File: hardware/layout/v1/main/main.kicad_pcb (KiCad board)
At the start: 4 copper layers, 32 x 52 mm, 47 parts, among them J1 12-32V + RS485, J2 Crown board, J3 Probe board, J4 PMSA003I PM, J5 Power board, Q1 AO3400A, SW1 SERVICE, U2 LM66100, U3 XIAO ESP32C6, U4 ADS1115IDGSR, U5 LSM6DS3TR-C, U7 SP3485EN-L/TR

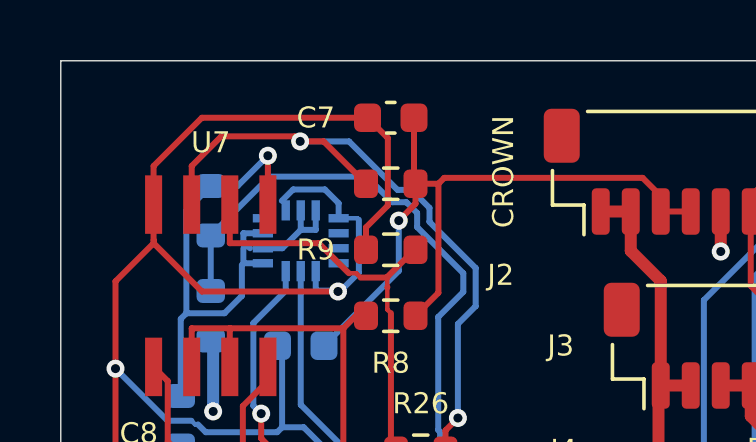
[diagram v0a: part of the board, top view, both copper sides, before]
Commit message: Update dome PCB to Genicom GUVB-C21SD/GUVA-C22SD photodiodes with TLV9062 transimpedance and ADS1115 ADC, increase diameter to Ø 15.6 mm
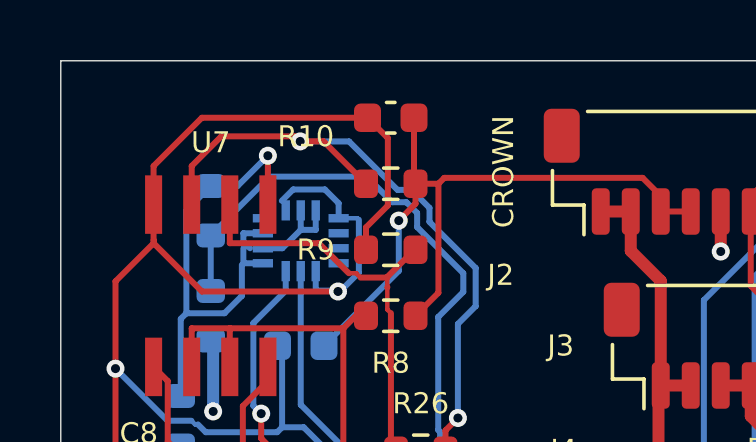
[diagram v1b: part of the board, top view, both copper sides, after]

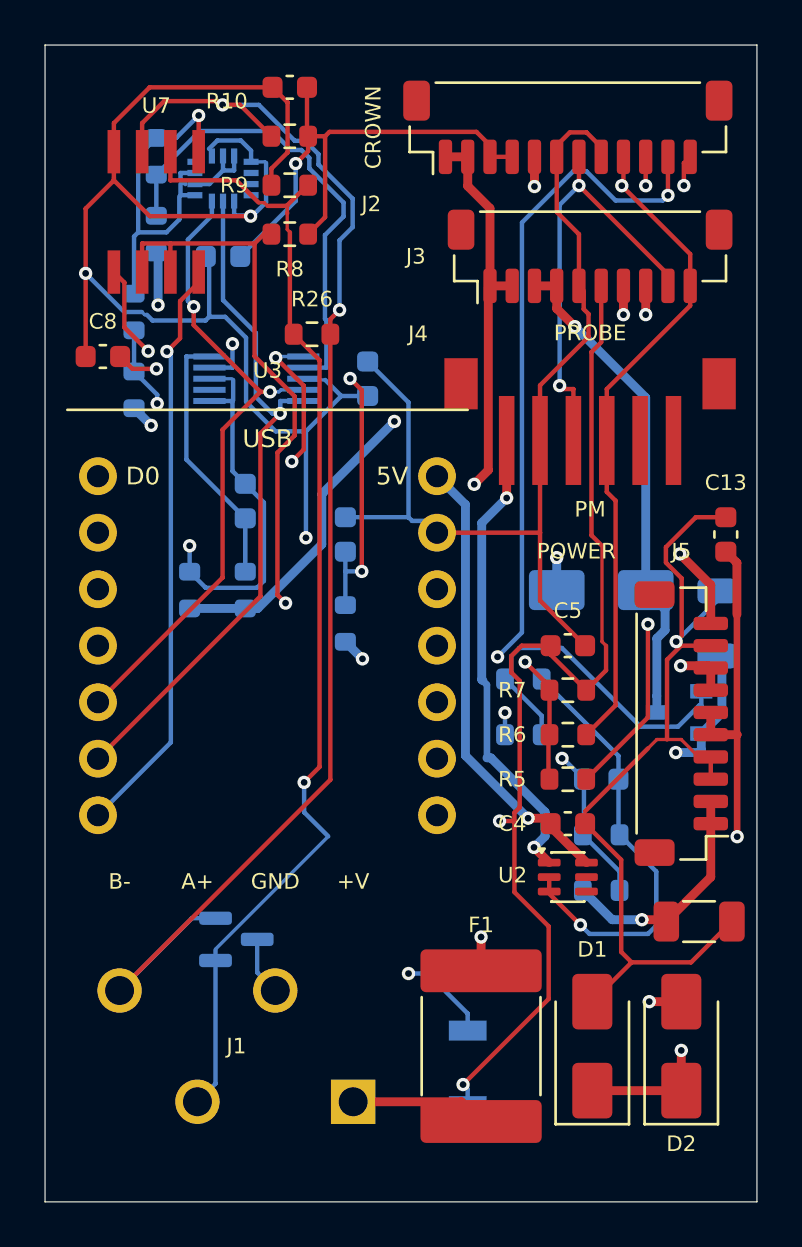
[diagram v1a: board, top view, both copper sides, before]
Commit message: Update dome PCB layout with manual reference and label placement, add Stock_Optional field for LTR-390UV-01 sensor to allow JLC assembly when in stock without failing release on shortage
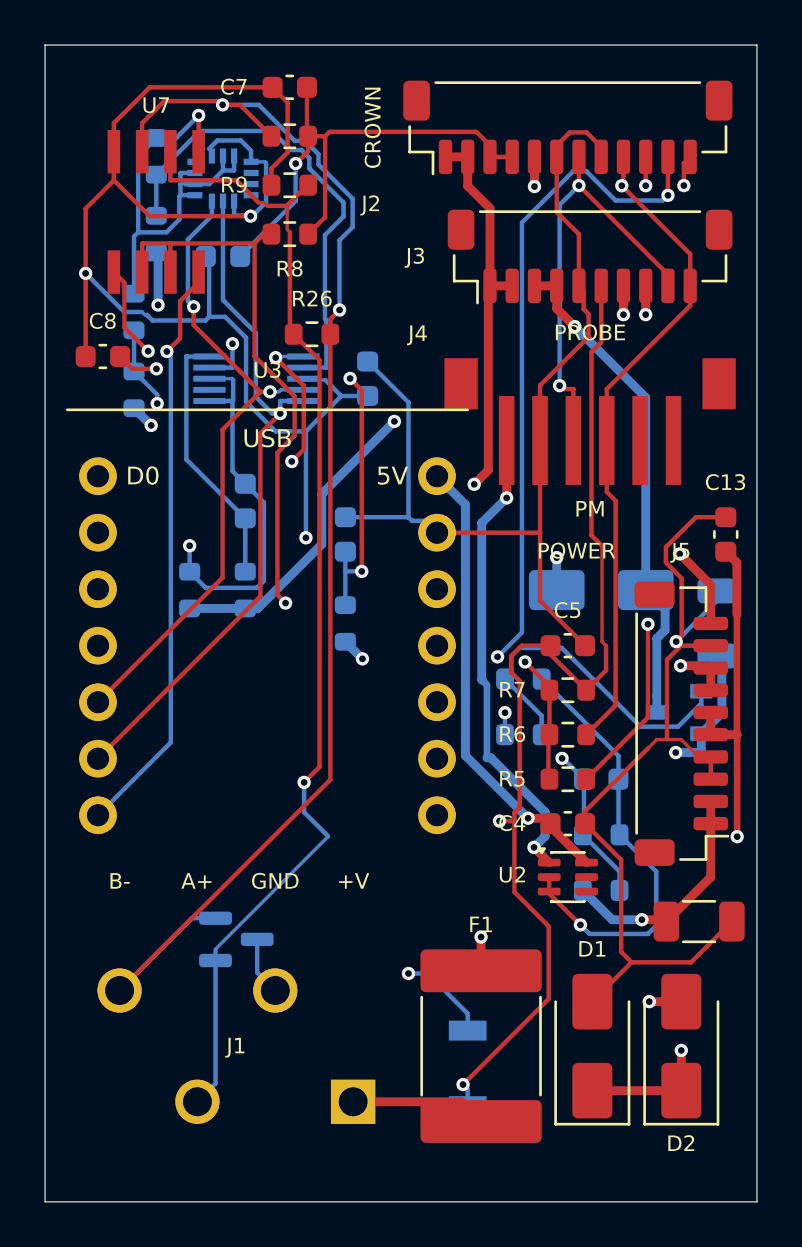
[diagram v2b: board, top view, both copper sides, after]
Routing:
- net GND: track 169.1 -> 170.9 mm

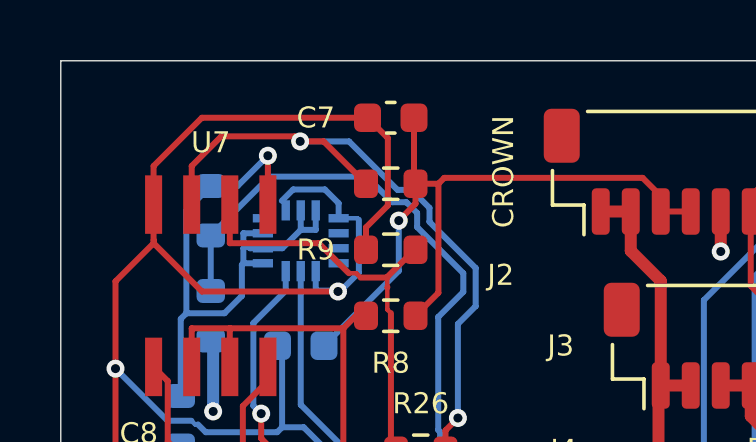
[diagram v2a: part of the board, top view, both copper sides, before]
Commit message: Update AS3935 lightning antenna to dual land pattern supporting Coilcraft MA5532-AE or Premo SDTR1103-HF1-0100J with adjusted Q damping resistor notes, and reorganize self-assembly order files to LCSC-only and elsewhere CSVs with multi-distributor columns
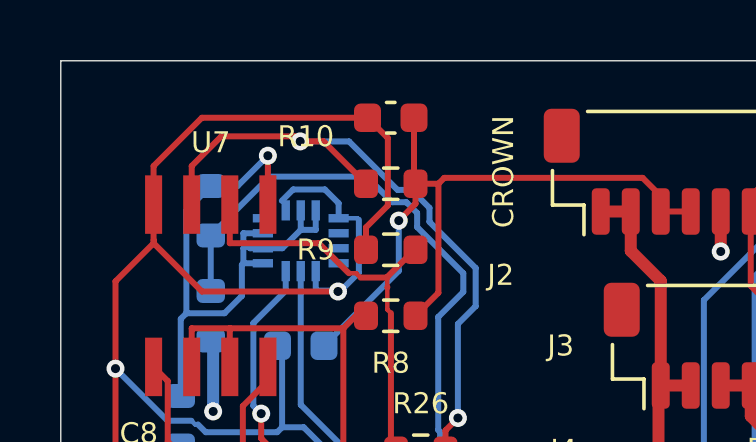
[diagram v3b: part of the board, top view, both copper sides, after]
